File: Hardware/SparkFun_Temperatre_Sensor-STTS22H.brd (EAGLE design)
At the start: 25.4 x 25.4 mm, 43 parts, among them J1 QWIIC_RIGHT_ANGLE, J2 QWIIC_RIGHT_ANGLE, U2 STTS22H

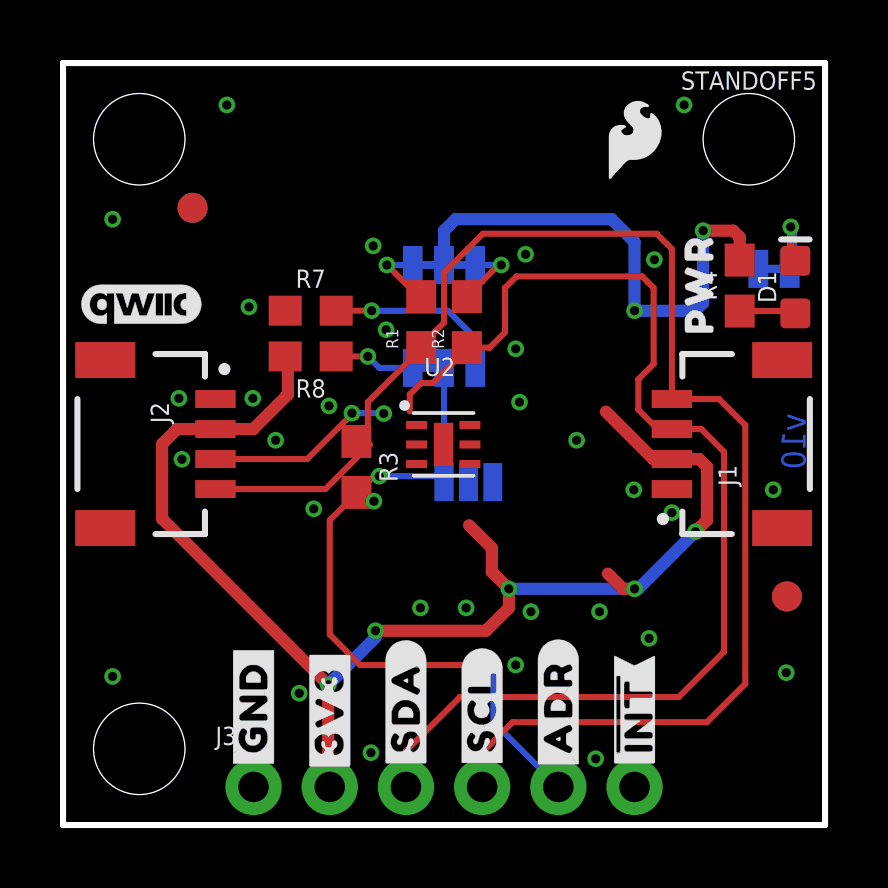
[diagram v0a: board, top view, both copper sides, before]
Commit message: Removes ADDR pin from header
* Routes board
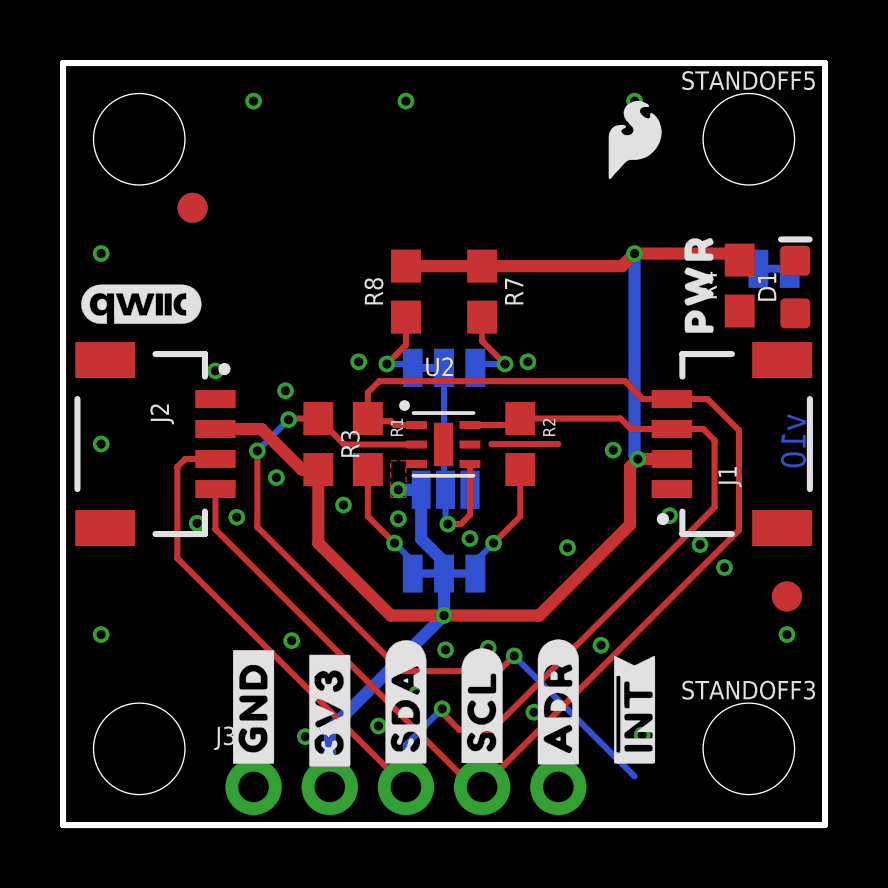
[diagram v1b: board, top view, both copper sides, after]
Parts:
- removed U$23: (no value), top:#POCI#16020
- removed U$24: (no value), top:#PICO#16021
- removed U$7: (no value), top:#SCLK#16021
- added STANDOFF3: STAND-OFFTIGHT, SparkFun-Hardware:STAND-OFF-TIGHT
- J3: device SparkFun-Connectors:1X06_NO_SILK -> SparkFun-Connectors:1X05_NO_SILK
- moved LOGO3 12.7 mm to (12.7, 21.4)
- moved I2C_PU 10.3 mm to (12.7, 8.38)
- moved U$25 10.2 mm to (12.7, 6.99)
- moved R7 5.75 mm to (14.0, 17.8), turned to 270 degrees
- moved R1 4.44 mm to (10.2, 12.7), turned to 270 degrees
- moved R2 4.44 mm to (15.2, 12.7), turned to 270 degrees
- moved R8 3.84 mm to (11.4, 17.8), turned to 90 degrees
- moved R3 1.48 mm to (8.51, 12.7)
- moved ADDR1 0.80 mm to (12.8, 11.2)
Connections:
- net !INT!: now also J3.5; no longer J3.6
- net ADDR: no longer J3.5
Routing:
- net !INT!: track 0.00 -> 25.1 mm, vias 0 -> 3
- net ADDR: track 22.5 -> 7.82 mm, vias 2 -> 1
- net 3.3V: track 62.1 -> 53.4 mm, vias 7 -> 4
- net SCL: track 48.2 -> 45.0 mm
- net SDA: track 45.3 -> 42.1 mm, vias 2 -> 1
- net N$7: track 6.01 -> 2.92 mm
- net N$3: track 2.68 -> 0.00 mm, vias 1 -> 0
- net GND: track 0.00 -> 2.24 mm, vias 32 -> 31
- net N$2: track 1.89 -> 0.00 mm
- net N$6: track 2.44 -> 4.09 mm
- net N$5: track 2.44 -> 4.09 mm
- added copper zone on layer 1, net 3.3V

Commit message: Adds silk
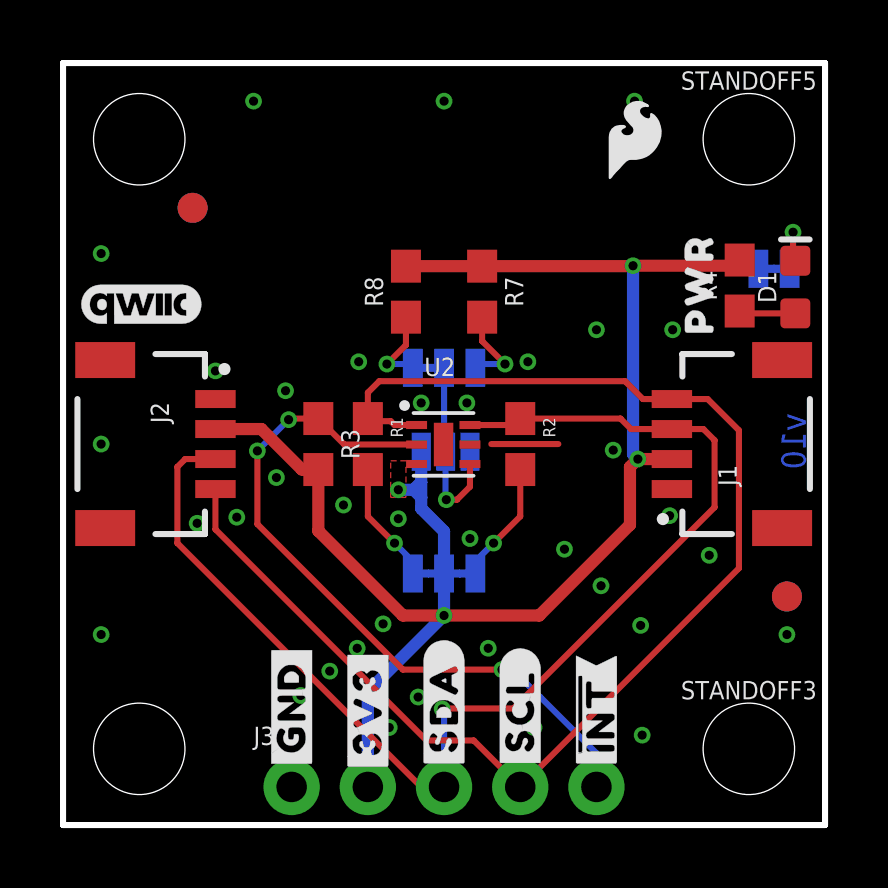
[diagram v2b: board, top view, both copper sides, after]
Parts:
- added U$12: (no value), top:#0X3C#25
- added U$13: (no value), top:#0X3E#25
- added U$14: (no value), top:#0X3F#25
- added U$15: (no value), top:#0X38#25
- added U$17: (no value), top:TEMPERATURE23
- added U$19: (no value), top:SENSOR24
- added U$22: (no value), top:STTS22H21
- added U$5: (no value), top:#SDA#7
- added U$7: (no value), top:#SCL#6
- U$8: device bot:#ADR#441018 -> top:#ADDR1#9
- moved U$8 7.84 mm to (12.9, 10.9), flipped to the bottom, turned to 0 degrees
- moved U$6 3.10 mm to (12.7, 16.8)
- moved J3 1.27 mm to (7.62, 1.27)
- moved U$1 1.27 mm to (7.62, 3.94)
- moved U$9 1.27 mm to (7.62, 3.94)
- moved ADDR1 1.27 mm to (12.8, 12.4)
- moved U$10 1.27 mm to (10.2, 3.81)
- moved U$11 1.27 mm to (17.8, 3.68)
- moved U$18 1.27 mm to (17.8, 3.68)
- moved U$2 1.27 mm to (10.2, 3.81)
- moved U$3 1.27 mm to (12.7, 3.94)
- moved U$4 1.27 mm to (15.2, 3.81)
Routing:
- net N$3: track 0.00 -> 2.25 mm, vias 0 -> 1
- net N$2: track 0.00 -> 1.89 mm
- net ADDR: track 7.82 -> 6.15 mm
- net !INT!: track 25.1 -> 24.1 mm
- net SCL: track 45.0 -> 45.8 mm
- net GND: vias 31 -> 37

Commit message: Adds decoupling cap which resulted in additional routing
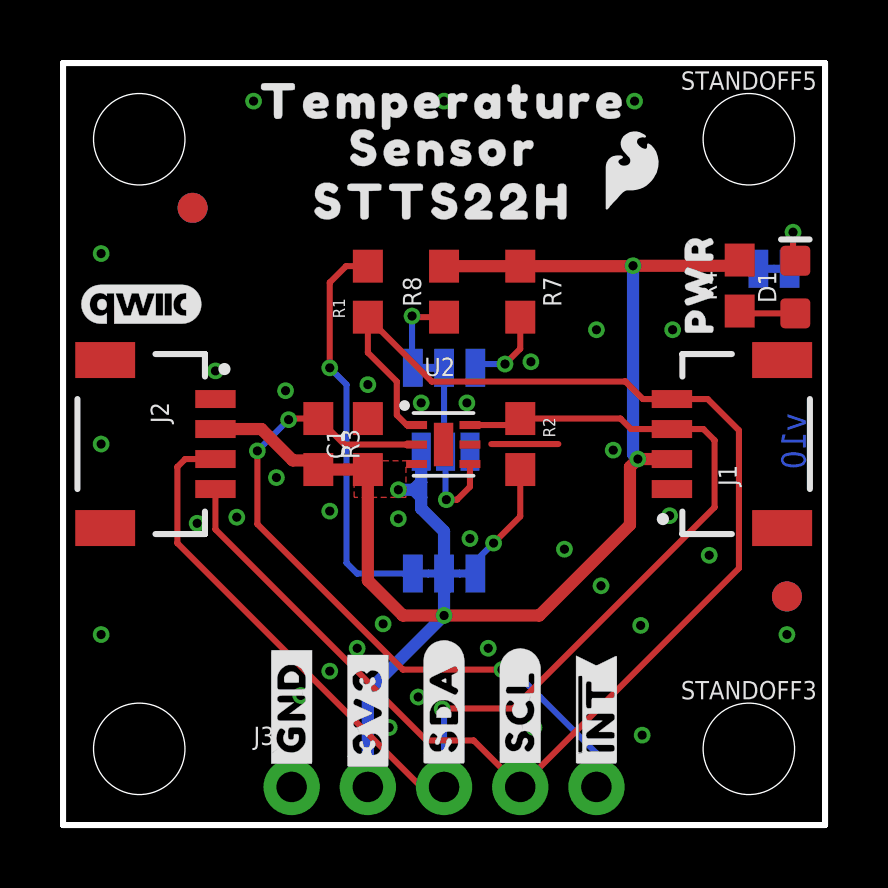
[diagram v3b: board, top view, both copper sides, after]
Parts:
- added C1: 0.1uF, SparkFun-Capacitors:0603
- added U$23: (no value), top:TEMPERATURE23
- added U$24: (no value), top:SENSOR24
- added U$26: (no value), top:STTS22H21
- moved R1 5.08 mm to (10.2, 17.8), turned to 90 degrees
- moved R7 1.27 mm to (15.2, 17.8)
- moved R8 1.27 mm to (12.7, 17.8)
- moved U$20 1.02 mm to (18.9, 21.8)
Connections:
- net 3.3V: now also C1.1
- net GND: now also C1.2
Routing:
- net N$5: track 4.09 -> 13.8 mm
- net SCL: track 45.8 -> 48.4 mm
- net N$4: track 2.74 -> 3.34 mm
